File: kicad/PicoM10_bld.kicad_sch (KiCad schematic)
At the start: 20 parts, among them J1 Conn_Coaxial, U1 MIA-M10Q, U2 NCP160xMX

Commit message: minor cleanup and updates
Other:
- note added: "4x 10uF 10V 0402"
- note added: "D1: min 20V; 100 mA"
- note added: "board-level decoupling this will ONLY work with the right stackup!"
- note removed: "C1, C3: 10uF 10V 0402"
- note removed: "board-level decoupling"
- moved on the sheet: C2, C3, C4, C5, C6, D1, R1, TP1, TP2, TP3, TP4

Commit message: minor update
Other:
- company: (none) -> MakerProbe - Christoph Redecker
- title: (none) -> Pico-M10
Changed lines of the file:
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@@
 	(generator_version "8.0")
 	(paper "A4")
+	(title_block
+		(title "Pico-M10")
+		(date "2024-11-04")
+		(rev "0.1 draft")
+		(company "MakerProbe - Christoph Redecker")
+	)
 	(junction
 		(at 187.96 113.03)

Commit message: minor schematic and layout updates
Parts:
- C1, C2, C3, C4, C5: MPN (none) -> GRM155R61A106ME1D
- C6: MPN (none) -> T520A107M06ATE045
- J1: MPN (none) -> CONMHF1-SMD-G-T
- U1: MPN (none) -> MIA-M10Q
- U2: value NCP160xMX -> NCP160AMX330TBG; MPN (none) -> NCP160AMX330TBG
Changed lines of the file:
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@@
+			)
+		)
+		(property "MPN" ""
+			(at 125.73 74.93 0)
+			(effects
+				(font
+					(size 1.27 1.27)
+				)
+				(hide yes)
 			)
 		)
@@
 			)
 		)
+		(property "MPN" "GRM155R61A106ME1D"
+			(at 39.37 160.02 0)
+			(effects
+				(font
+					(size 1.27 1.27)
+				)
+				(hide yes)
+			)
+		)
 		(pin "1"
 		)
@@
 		)
 		(property "Description" "Light emitting diode"
+			(at 236.22 87.63 0)
+			(effects
+				(font
+					(size 1.27 1.27)
+				)
+				(hide yes)
+			)
+		)
+		(property "MPN" ""
 			(at 236.22 87.63 0)
 			(effects
@@
 			)
 		)
+		(property "MPN" "CONMHF1-SMD-G-T"
+			(at 104.14 74.93 0)
+			(effects
+				(font
+					(size 1.27 1.27)
+				)
+				(hide yes)
+			)
+		)
 		(pin "2"
 		)
@@
 		)
 		(property "Description" ""
+			(at 185.42 88.9 0)
+			(effects
+				(font
+					(size 1.27 1.27)
+				)
+				(hide yes)
+			)
+		)
+		(property "MPN" "MIA-M10Q"
 			(at 185.42 88.9 0)
 			(effects
@@
 			)
 		)
+		(property "MPN" ""
+			(at 34.29 110.49 0)
+			(effects
+				(font
+					(size 1.27 1.27)
+				)
+				(hide yes)
+			)
+		)
 		(pin "1"
 		)
@@
 		(on_board yes)
 		(dnp no)
-		(fields_autoplaced yes)
 		(property "Reference" "C3"
 			(at 31.75 158.7562 0)
@@
 			)
 		)
+		(property "MPN" "GRM155R61A106ME1D"
+			(at 40.64 174.498 0)
+			(effects
+				(font
+					(size 1.27 1.27)
+				)
+			)
+		)
 		(pin "1"
 		)
@@
 		(on_board yes)
 		(dnp no)
-		(fields_autoplaced yes)
 		(property "Reference" "C6"
 			(at 77.47 157.8609 0)
@@
 			)
 		)
+		(property "MPN" "T520A107M06ATE045 "
+			(at 78.486 173.99 0)
+			(effects
+				(font
+					(size 1.27 1.27)
+				)
+			)
+		)
 		(pin "1"
 		)
@@
 		)
 		(property "Description" "Inductor, small symbol"
+			(at 134.62 80.01 0)
+			(effects
+				(font
+					(size 1.27 1.27)
+				)
+				(hide yes)
+			)
+		)
+		(property "MPN" ""
 			(at 134.62 80.01 0)
 			(effects
@@
 			)
 		)
+		(property "MPN" ""
+			(at 34.29 92.71 0)
+			(effects
+				(font
+					(size 1.27 1.27)
+				)
+				(hide yes)
+			)
+		)
 		(pin "1"
 		)
@@
 			)
 		)
-		(property "Value" "NCP160xMX"
+		(property "Value" "NCP160AMX330TBG"
 			(at 48.26 39.37 0)
 			(effects
@@
 			)
 		)
+		(property "MPN" "NCP160AMX330TBG"
+			(at 48.26 48.26 0)
+			(effects
+				(font
+					(size 1.27 1.27)
+				)
+				(hide yes)
+			)
+		)
 		(pin "3"
 		)
@@
 		)
 		(property "Description" "Unpolarized capacitor, small symbol"
+			(at 27.94 49.53 0)
+			(effects
+				(font
+					(size 1.27 1.27)
+				)
+				(hide yes)
+			)
+		)
+		(property "MPN" "GRM155R61A106ME1D"
 			(at 27.94 49.53 0)
 			(effects
@@
 			)
 		)
+		(property "MPN" ""
+			(at 34.29 104.14 0)
+			(effects
+				(font
+					(size 1.27 1.27)
+				)
+				(hide yes)
+			)
+		)
 		(pin "1"
 		)
@@
 			)
 		)
+		(property "MPN" ""
+			(at 34.29 86.36 0)
+			(effects
+				(font
+					(size 1.27 1.27)
+				)
+				(hide yes)
+			)
+		)
 		(pin "1"
 		)
@@
 			)
 		)
+		(property "MPN" "GRM155R61A106ME1D"
+			(at 49.53 160.02 0)
+			(effects
+				(font
+					(size 1.27 1.27)
+				)
+				(hide yes)
+			)
+		)
 		(pin "1"
 		)
@@
 			)
 		)
+		(property "MPN" "GRM155R61A106ME1D"
+			(at 59.69 160.02 0)
+			(effects
+				(font
+					(size 1.27 1.27)
+				)
+				(hide yes)
+			)
+		)
 		(pin "1"
 		)
@@
 			)
 		)
+		(property "MPN" ""
+			(at 116.84 80.01 0)
+			(effects
+				(font
+					(size 1.27 1.27)
+				)
+				(hide yes)
+			)
+		)
 		(pin "1"
 		)
@@
 		)
 		(property "Description" "Resistor, small symbol"
+			(at 57.15 105.41 0)
+			(effects
+				(font
+					(size 1.27 1.27)
+				)
+				(hide yes)
+			)
+		)
+		(property "MPN" ""
 			(at 57.15 105.41 0)
 			(effects
@@
 			)
 		)
+		(property "MPN" ""
+			(at 236.22 97.79 0)
+			(effects
+				(font
+					(size 1.27 1.27)
+				)
+				(hide yes)
+			)
+		)
 		(pin "2"
 		)
@@
 			(at 54.61 87.63 0)
 			(effects
+				(font
+					(size 1.27 1.27)
+				)
+				(hide yes)
+			)
+		)
+		(property "MPN" ""
+			(at 54.61 87.63 0)
+			(effects

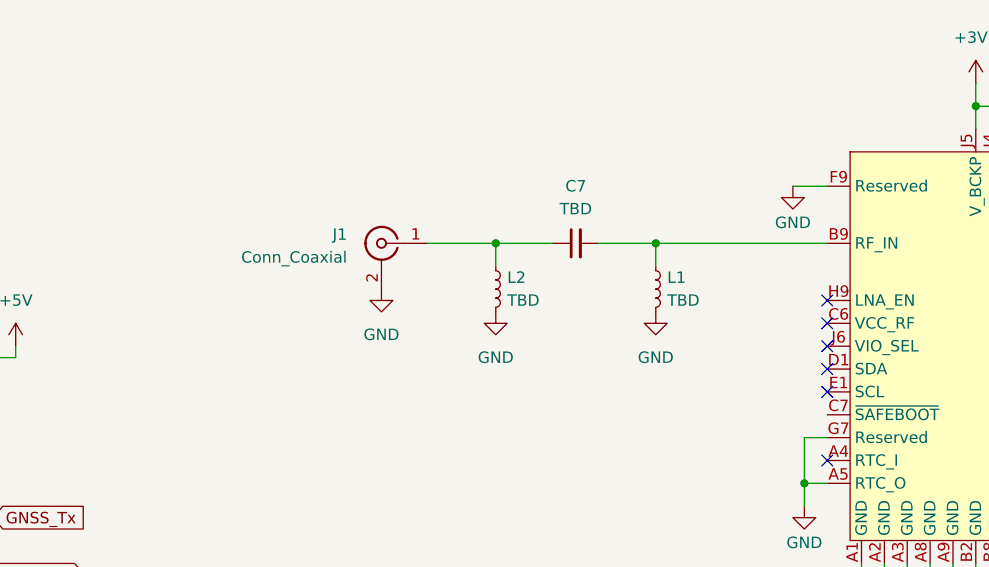
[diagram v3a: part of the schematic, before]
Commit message: add TVS diode
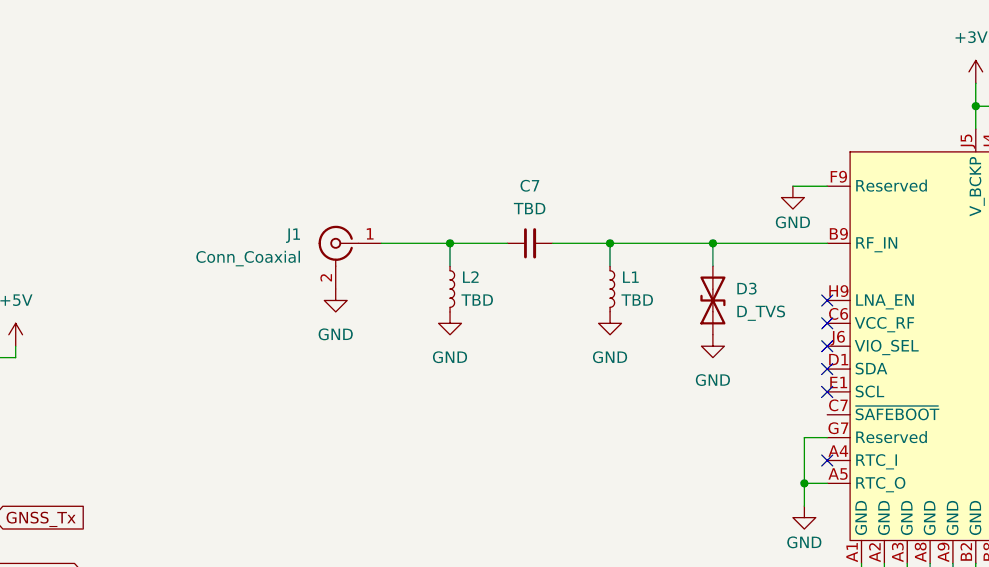
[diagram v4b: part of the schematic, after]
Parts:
- added D3: D_TVS, Diode_SMD:Nexperia_DSN0603-2_0.6x0.3mm_P0.4mm, symbol Device:D_TVS
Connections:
- net GND: now also D3.1 (A1)
- net at C7.2, L1.1, U1.B9 (RF_IN): now also D3.2 (A2)
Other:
- moved on the sheet: C7, J1, L1, L2

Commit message: updates
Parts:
- added D4, D5, D6: PESD3V3Z1BSF, Diode_SMD:Nexperia_DSN0603-2_0.6x0.3mm_P0.4mm, symbol Device:D_TVS
- added TP5: Safeboot, TestPoint:TestPoint_Pad_D1.0mm, symbol Connector:TestPoint_Flag
- D3: value D_TVS -> PESD3V3Z1BSF; MPN (none) -> PESD3V3Z1BSF
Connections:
- net GND: now also D4.1 (A1), D5.1 (A1), D6.1 (A1)
- net GNSS_Rx: now also D5.2 (A2)
- net at U1.C7 (~{SAFEBOOT}): now also D6.2 (A2), TP5.1
- net at R1.1, TP3.1: now also D4.2 (A2)
- no-connect marks 8 -> 9
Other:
- moved on the sheet: D2, R1, R2, U1
